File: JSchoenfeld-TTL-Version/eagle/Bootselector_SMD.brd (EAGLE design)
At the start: 21 x 51.4 mm, 13 parts, among them IC3 74HCT00D, IC4 74HCT157D

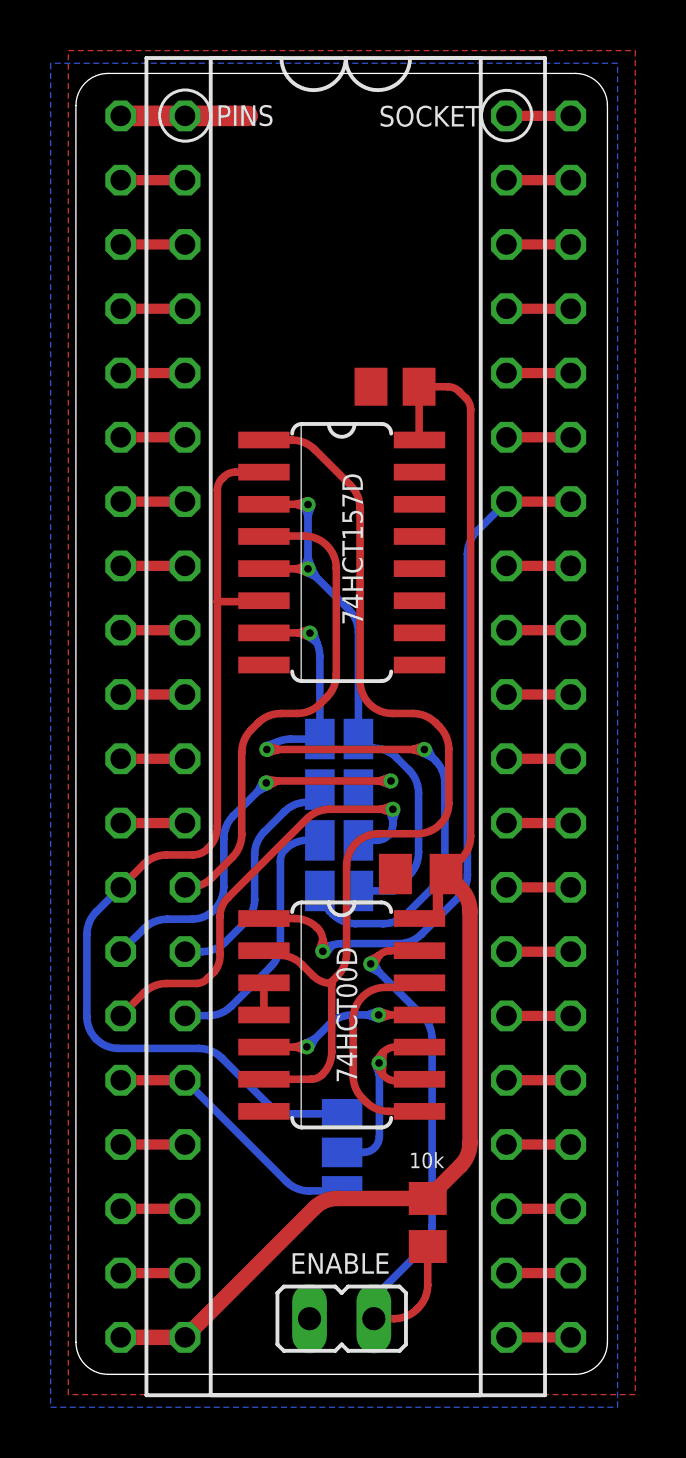
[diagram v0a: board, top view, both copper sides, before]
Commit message: 25.02.2018 - Fredric QJ Blåholtz (e5frog) + Marko Oette (marko@oette.info) v. 0.98 - Prototyping v 0.97 done, works - Updated SMD version to match THT version - Updated documentation for THT version - Added mouse enable / disable documentation
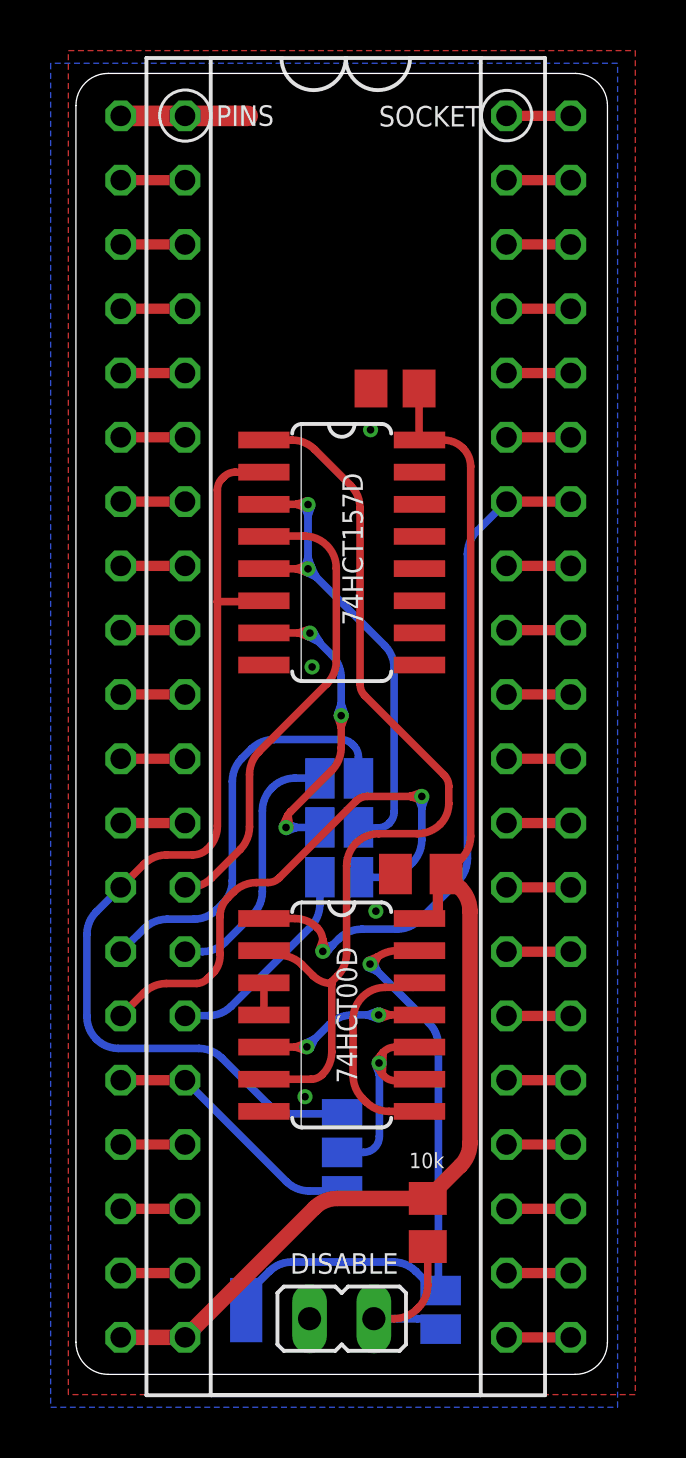
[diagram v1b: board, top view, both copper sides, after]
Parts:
- removed SJ4: (no value), jumper:SJ
- added EXT: (no value), wirepad:SMD1,27-2,54
- added SJX: (no value), jumper:SJ
- DISABLE: value on/off -> Leave open for swap
- moved SJ3 19.0 mm to (14.4, 2.55), turned to 90 degrees
- moved SJ2 3.46 mm to (10.4, 19.6)
- moved SJ1 1.56 mm to (10.4, 23.5)
- moved C1 0.07 mm to (12.6, 39.0)
- renumbered ENABLE to DISABLE
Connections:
- net /TRGSEL renamed !TRGSEL
- removed net N$2: DISABLE.1, IC3.13, R1.1
- new net N$1: EXT.1, IC3.13, SJ3.2
- new net N$23: DISABLE.1, R1.1, SJ3.1
- net !NEWSEL1: now also SJ1.2; no longer SJ2.2
- net !NEWSEL2: now also SJ2.2; no longer SJ3.2
- net !NEWSELX: now also SJX.2; no longer SJ1.2, SJ4.2
- net !SEL1: now also SJ1.1; no longer SJ2.1
- net !SEL2: now also SJ2.1; no longer SJ3.1
- net !SELX: now also SJX.1; no longer SJ1.1, SJ4.1
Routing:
- net N$1: track 0.00 -> 27.3 mm, vias 0 -> 1
- net N$2: track 24.8 -> 0.00 mm, vias 1 -> 0
- net !NEWSELX: track 32.9 -> 19.5 mm
- net N$23: track 0.00 -> 7.29 mm
- net !SEL2: track 19.7 -> 24.7 mm
- net !SEL1: track 21.0 -> 16.6 mm, vias 2 -> 0
- net !SELX: track 28.2 -> 24.5 mm
- net VCC: track 54.3 -> 52.1 mm
- net !NEWSEL2: track 10.3 -> 8.37 mm
- net !NEWSEL1: track 9.31 -> 10.3 mm
- net !NEWSEL0: track 19.4 -> 18.6 mm
- net SEL_ENABLE: track 37.9 -> 37.2 mm
- net GND: vias 0 -> 4
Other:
- board text added: "!S3! | !S0"
- board text added: "Amiga Bootselector Licensed under GPL v. 2 See: http://retro.oette.info J. Schoenfeld - www.c64.de Artwork by o.eschi/moette/e5frog"
- board text added: "BRIDGE !S0 IF A1000 KS <= 1.3"
- board text added: "ELSE BRIDGE !S3"
- board text added: "N1"
- board text added: "N2"
- board text added: "NX"
- board text added: "S1"
- board text added: "S2"
- board text added: "SWAP DF0:~DF1:"
- board text added: "SWAP DF0:~DF2:"
- board text added: "SX"
- board text added: "e5frog 2018"
- board text removed: "!SEL0! | !SEL3"
